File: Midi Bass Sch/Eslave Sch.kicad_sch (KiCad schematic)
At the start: 1 part

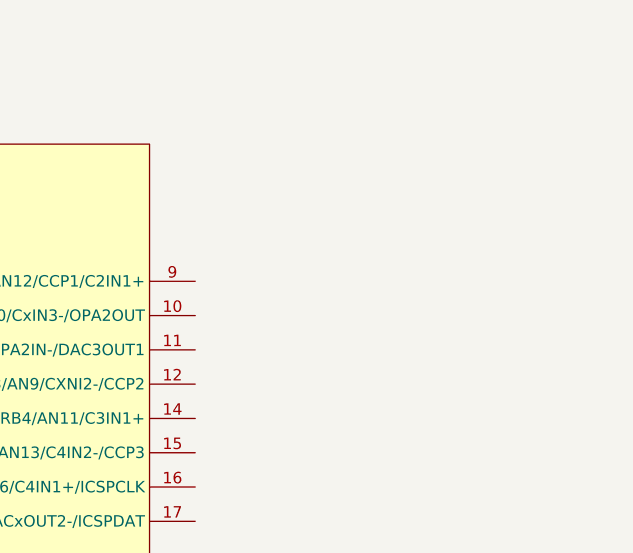
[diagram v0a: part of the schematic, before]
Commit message: reduced time of pulse
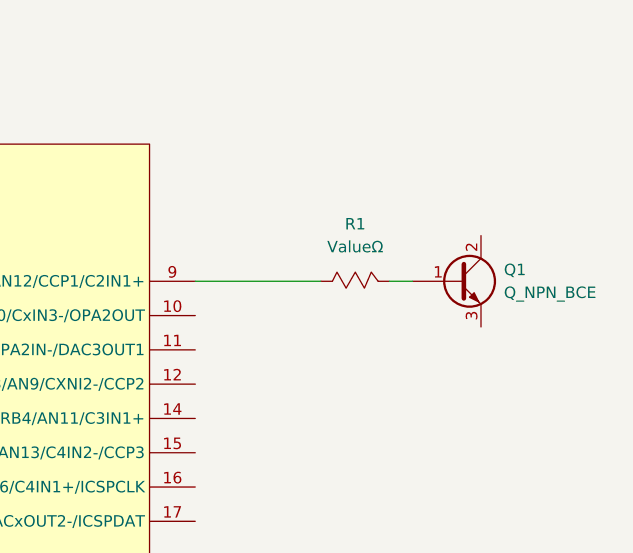
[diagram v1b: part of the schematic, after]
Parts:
- added Q1: Q_NPN_BCE, symbol Device:Q_NPN_BCE
- added R1: ValueΩ, symbol Custom Symbols:Resistor_Mod
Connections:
- net at U?.9 (RB0/AN12/CCP1/C2IN1+): now also R1.1
- new net: Q1.1 (B), R1.2
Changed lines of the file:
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@@
+	(wire
+		(pts
+			(xy 210.82 46.99) (xy 213.36 46.99)
+		)
+		(stroke
+			(width 0)
+			(type default)
+		)
+	)
 	(wire
 		(pts
@@
 		(pts
 			(xy 152.4 156.21) (xy 152.4 154.94)
+		)
+		(stroke
+			(width 0)
+			(type default)
+		)
+	)
+	(wire
+		(pts
+			(xy 189.23 46.99) (xy 203.2 46.99)
 		)
 		(stroke
@@
 				(justify right)
 				(hide yes)
+			)
+		)
+	)
+	(symbol
+		(lib_id "Custom Symbols:Resistor_Mod")
+		(at 207.01 46.99 0)
+		(unit 1)
+		(exclude_from_sim no)
+		(in_bom yes)
+		(on_board yes)
+		(dnp no)
+		(fields_autoplaced yes)
+		(property "Reference" "R1"
+			(at 207.01 40.64 0)
+			(effects
+				(font
+					(size 1.27 1.27)
+				)
+			)
+		)
+		(property "Value" "ValueΩ"
+			(at 207.01 43.18 0)
+			(effects
+				(font
+					(size 1.27 1.27)
+				)
+			)
+		)
+		(property "Footprint" ""
+			(at 205.74 44.45 0)
+			(effects
+				(font
+					(size 1.27 1.27)
+				)
+				(hide yes)
+			)
+		)
+		(property "Datasheet" ""
+			(at 205.74 44.45 0)
+			(effects
+				(font
+					(size 1.27 1.27)
+				)
+				(hide yes)
+			)
+		)
+		(property "Description" ""
+			(at 207.01 46.99 0)
+			(effects
+				(font
+					(size 1.27 1.27)
+				)
+				(hide yes)
+			)
+		)
+		(pin "2"
+		)
+		(pin "1"
+		)
+		(instances
+			(project ""
+				(path "/06818073-fb22-48ee-acc5-6dedd827034e/55f5fc9c-362b-429f-ad6f-f98ffe4c4860"
+					(reference "R1")
+					(unit 1)
+				)
 			)
 		)
@@
 					(unit 1)
 				)
+			)
+		)
+	)
+	(symbol
+		(lib_id "Device:Q_NPN_BCE")
+		(at 218.44 46.99 0)
+		(unit 1)
+		(exclude_from_sim no)
+		(in_bom yes)
+		(on_board yes)
+		(dnp no)
+		(fields_autoplaced yes)
+		(property "Reference" "Q1"
+			(at 223.52 45.7199 0)
+			(effects
+				(font
+					(size 1.27 1.27)
+				)
+				(justify left)
+			)
+		)
+		(property "Value" "Q_NPN_BCE"
+			(at 223.52 48.2599 0)
+			(effects
+				(font
+					(size 1.27 1.27)
+				)
+				(justify left)
+			)
+		)
+		(property "Footprint" ""
+			(at 223.52 44.45 0)
+			(effects
+				(font
+					(size 1.27 1.27)
+				)
+				(hide yes)
+			)
+		)
+		(property "Datasheet" "~"
+			(at 218.44 46.99 0)
+			(effects
+				(font
+					(size 1.27 1.27)
+				)
+				(hide yes)
+			)
+		)
+		(property "Description" "NPN transistor, base/collector/emitter"
+			(at 218.44 46.99 0)
+			(effects
+				(font
+					(size 1.27 1.27)
+				)
+				(hide yes)
+			)
+		)
+		(pin "1"
+		)
+		(pin "2"
+		)
+		(pin "3"
+		)
+		(instances
+			(project ""
+				(path "/06818073-fb22-48ee-acc5-6dedd827034e/55f5fc9c-362b-429f-ad6f-f98ffe4c4860"
+					(reference "Q1")
+					(unit 1)
+				)

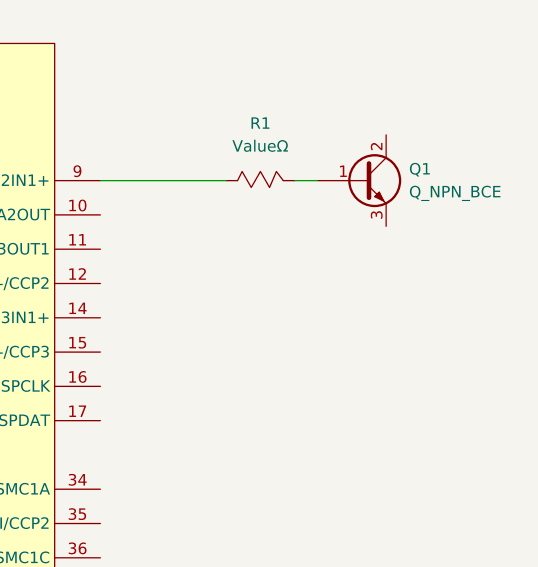
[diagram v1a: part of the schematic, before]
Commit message: updated schematic to include solenoid output
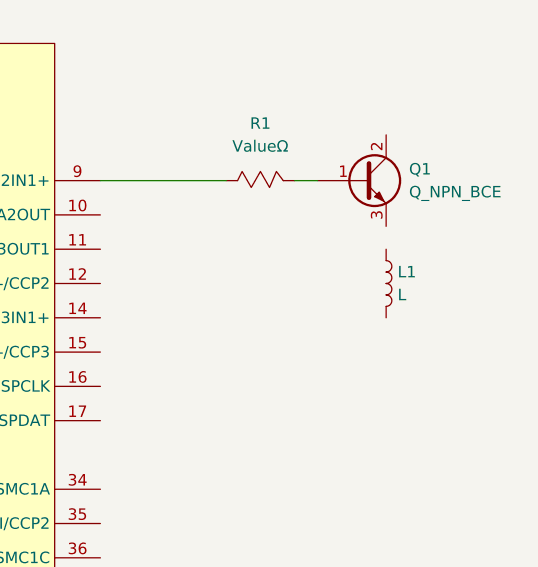
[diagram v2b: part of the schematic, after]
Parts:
- added L1: L, symbol Device:L
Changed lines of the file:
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@@
+	)
+	(symbol
+		(lib_id "Device:L")
+		(at 220.98 58.42 0)
+		(unit 1)
+		(exclude_from_sim no)
+		(in_bom yes)
+		(on_board yes)
+		(dnp no)
+		(fields_autoplaced yes)
+		(property "Reference" "L1"
+			(at 222.25 57.1499 0)
+			(effects
+				(font
+					(size 1.27 1.27)
+				)
+				(justify left)
+			)
+		)
+		(property "Value" "L"
+			(at 222.25 59.6899 0)
+			(effects
+				(font
+					(size 1.27 1.27)
+				)
+				(justify left)
+			)
+		)
+		(property "Footprint" ""
+			(at 220.98 58.42 0)
+			(effects
+				(font
+					(size 1.27 1.27)
+				)
+				(hide yes)
+			)
+		)
+		(property "Datasheet" "~"
+			(at 220.98 58.42 0)
+			(effects
+				(font
+					(size 1.27 1.27)
+				)
+				(hide yes)
+			)
+		)
+		(property "Description" "Inductor"
+			(at 220.98 58.42 0)
+			(effects
+				(font
+					(size 1.27 1.27)
+				)
+				(hide yes)
+			)
+		)
+		(pin "1"
+		)
+		(pin "2"
+		)
+		(instances
+			(project ""
+				(path "/06818073-fb22-48ee-acc5-6dedd827034e/55f5fc9c-362b-429f-ad6f-f98ffe4c4860"
+					(reference "L1")
+					(unit 1)
+				)
+			)
+		)
 	)
 	(symbol

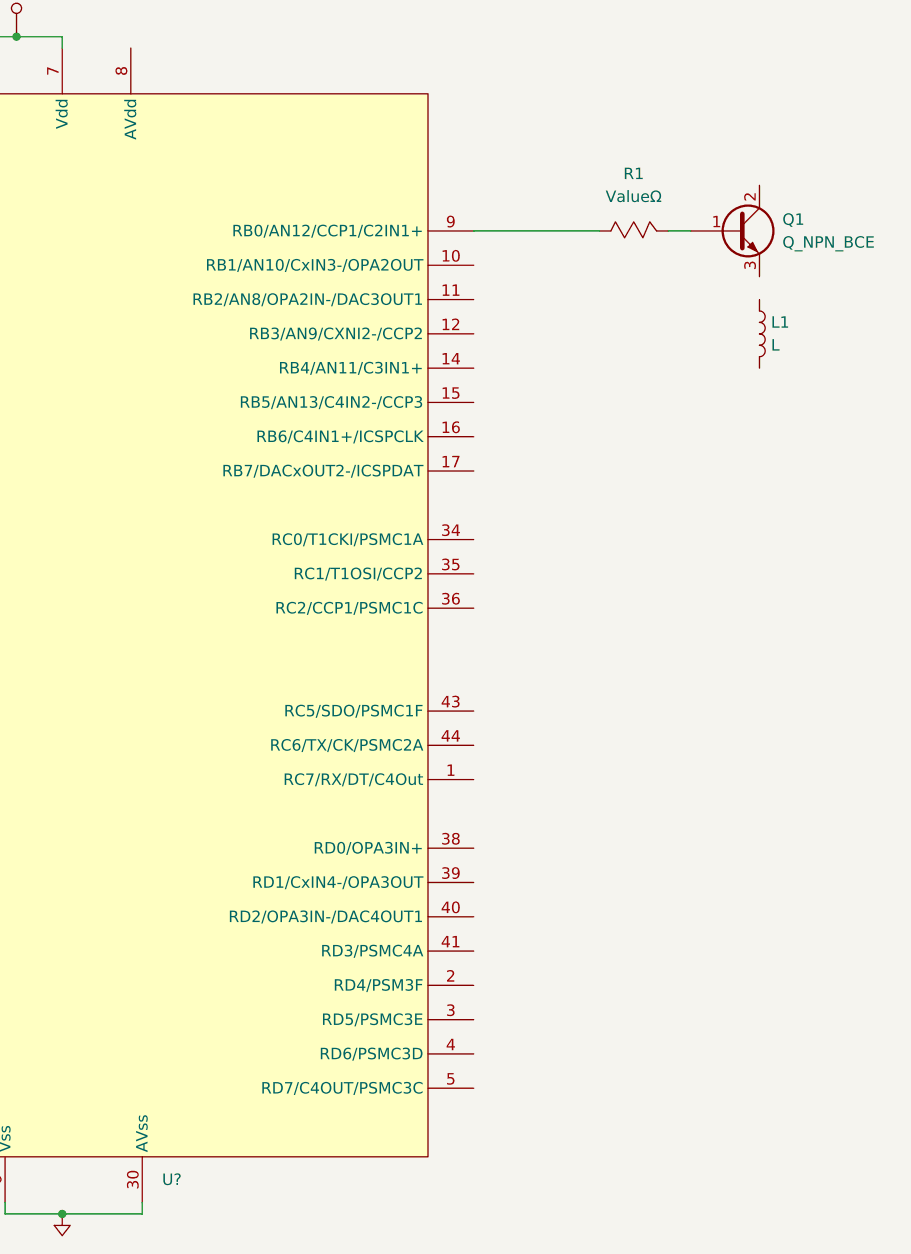
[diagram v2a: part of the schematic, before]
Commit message: updated schematic to include solenoids for pluck slave
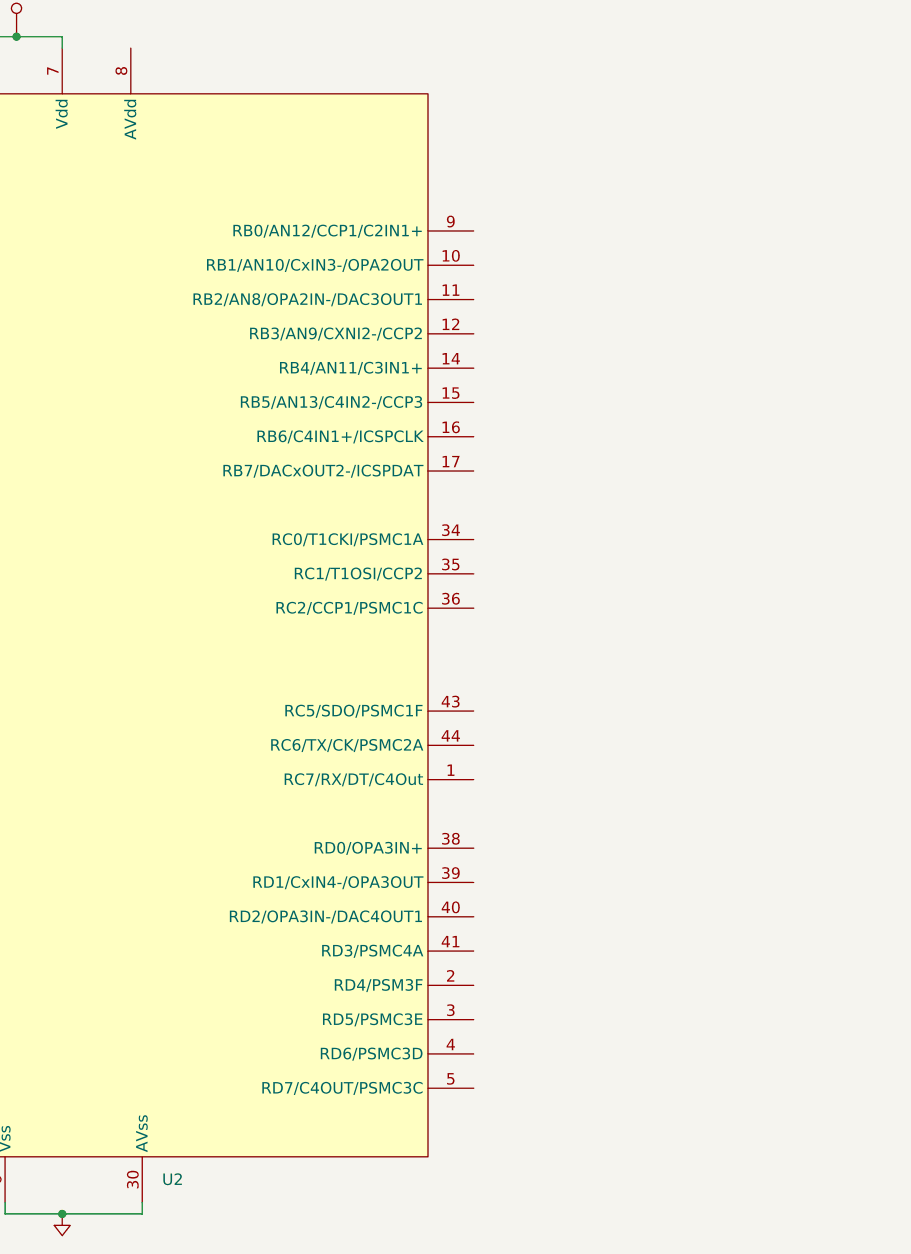
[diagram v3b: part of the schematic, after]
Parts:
- removed L1: L, symbol Device:L
- removed Q1: Q_NPN_BCE, symbol Device:Q_NPN_BCE
- removed R1: ValueΩ, symbol Custom Symbols:Resistor_Mod
- gave numbers to parts that had none: 1
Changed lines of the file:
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@@
-	(wire
-		(pts
-			(xy 210.82 46.99) (xy 213.36 46.99)
-		)
-		(stroke
-			(width 0)
-			(type default)
-		)
-	)
 	(wire
 		(pts
@@
 		(pts
 			(xy 152.4 156.21) (xy 152.4 154.94)
-		)
-		(stroke
-			(width 0)
-			(type default)
-		)
-	)
-	(wire
-		(pts
-			(xy 189.23 46.99) (xy 203.2 46.99)
 		)
 		(stroke
@@
 				(justify right)
 				(hide yes)
-			)
-		)
-	)
-	(symbol
-		(lib_id "Custom Symbols:Resistor_Mod")
-		(at 207.01 46.99 0)
-		(unit 1)
-		(exclude_from_sim no)
-		(in_bom yes)
-		(on_board yes)
-		(dnp no)
-		(fields_autoplaced yes)
-		(property "Reference" "R1"
-			(at 207.01 40.64 0)
-			(effects
-				(font
-					(size 1.27 1.27)
-				)
-			)
-		)
-		(property "Value" "ValueΩ"
-			(at 207.01 43.18 0)
-			(effects
-				(font
-					(size 1.27 1.27)
-				)
-			)
-		)
-		(property "Footprint" ""
-			(at 205.74 44.45 0)
-			(effects
-				(font
-					(size 1.27 1.27)
-				)
-				(hide yes)
-			)
-		)
-		(property "Datasheet" ""
-			(at 205.74 44.45 0)
-			(effects
-				(font
-					(size 1.27 1.27)
-				)
-				(hide yes)
-			)
-		)
-		(property "Description" ""
-			(at 207.01 46.99 0)
-			(effects
-				(font
-					(size 1.27 1.27)
-				)
-				(hide yes)
-			)
-		)
-		(pin "2"
-		)
-		(pin "1"
-		)
-		(instances
-			(project ""
-				(path "/06818073-fb22-48ee-acc5-6dedd827034e/55f5fc9c-362b-429f-ad6f-f98ffe4c4860"
-					(reference "R1")
-					(unit 1)
-				)
 			)
 		)
@@
 	)
 	(symbol
-		(lib_id "Device:L")
-		(at 220.98 58.42 0)
-		(unit 1)
-		(exclude_from_sim no)
-		(in_bom yes)
-		(on_board yes)
-		(dnp no)
-		(fields_autoplaced yes)
-		(property "Reference" "L1"
-			(at 222.25 57.1499 0)
-			(effects
-				(font
-					(size 1.27 1.27)
-				)
-				(justify left)
-			)
-		)
-		(property "Value" "L"
-			(at 222.25 59.6899 0)
-			(effects
-				(font
-					(size 1.27 1.27)
-				)
-				(justify left)
-			)
-		)
-		(property "Footprint" ""
-			(at 220.98 58.42 0)
-			(effects
-				(font
-					(size 1.27 1.27)
-				)
-				(hide yes)
-			)
-		)
-		(property "Datasheet" "~"
-			(at 220.98 58.42 0)
-			(effects
-				(font
-					(size 1.27 1.27)
-				)
-				(hide yes)
-			)
-		)
-		(property "Description" "Inductor"
-			(at 220.98 58.42 0)
-			(effects
-				(font
-					(size 1.27 1.27)
-				)
-				(hide yes)
-			)
-		)
-		(pin "1"
-		)
-		(pin "2"
-		)
-		(instances
-			(project ""
-				(path "/06818073-fb22-48ee-acc5-6dedd827034e/55f5fc9c-362b-429f-ad6f-f98ffe4c4860"
-					(reference "L1")
-					(unit 1)
-				)
-			)
-		)
-	)
-	(symbol
-		(lib_id "Device:Q_NPN_BCE")
-		(at 218.44 46.99 0)
-		(unit 1)
-		(exclude_from_sim no)
-		(in_bom yes)
-		(on_board yes)
-		(dnp no)
-		(fields_autoplaced yes)
-		(property "Reference" "Q1"
-			(at 223.52 45.7199 0)
-			(effects
-				(font
-					(size 1.27 1.27)
-				)
-				(justify left)
-			)
-		)
-		(property "Value" "Q_NPN_BCE"
-			(at 223.52 48.2599 0)
-			(effects
-				(font
-					(size 1.27 1.27)
-				)
-				(justify left)
-			)
-		)
-		(property "Footprint" ""
-			(at 223.52 44.45 0)
-			(effects
-				(font
-					(size 1.27 1.27)
-				)
-				(hide yes)
-			)
-		)
-		(property "Datasheet" "~"
-			(at 218.44 46.99 0)
-			(effects
-				(font
-					(size 1.27 1.27)
-				)
-				(hide yes)
-			)
-		)
-		(property "Description" "NPN transistor, base/collector/emitter"
-			(at 218.44 46.99 0)
-			(effects
-				(font
-					(size 1.27 1.27)
-				)
-				(hide yes)
-			)
-		)
-		(pin "1"
-		)
-		(pin "2"
-		)
-		(pin "3"
-		)
-		(instances
-			(project ""
-				(path "/06818073-fb22-48ee-acc5-6dedd827034e/55f5fc9c-362b-429f-ad6f-f98ffe4c4860"
-					(reference "Q1")
-					(unit 1)
-				)
-			)
-		)
-	)
-	(symbol
 		(lib_id "Owen's Symbols:PIC16F1789_44")
 		(at 143.51 31.75 0)
@@
 		(dnp no)
 		(fields_autoplaced yes)
-		(property "Reference" "U?"
+		(property "Reference" "U2"
 			(at 154.5941 152.4 0)
 			(effects
@@
 			(project "Midi Bass Sch"
 				(path "/06818073-fb22-48ee-acc5-6dedd827034e/55f5fc9c-362b-429f-ad6f-f98ffe4c4860"
-					(reference "U?")
+					(reference "U2")
 					(unit 1)
 				)

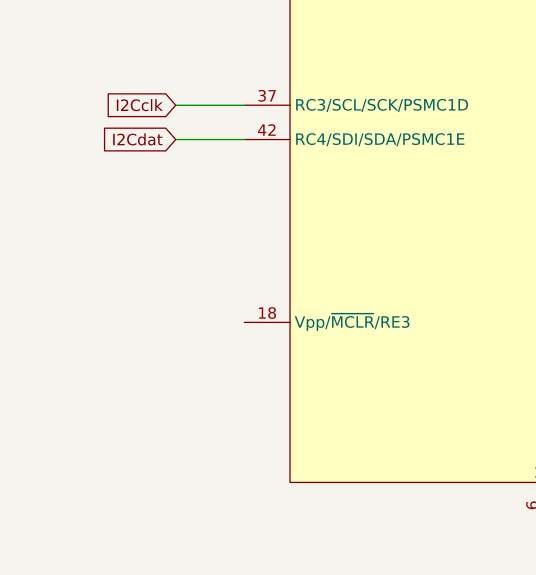
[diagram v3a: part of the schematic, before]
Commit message: added startup clear to schematic
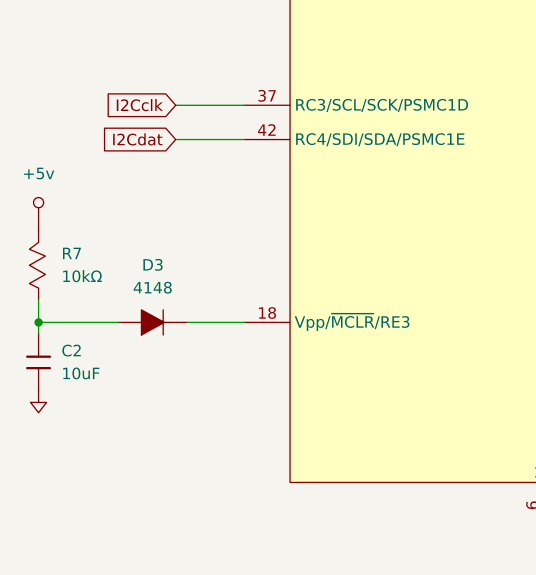
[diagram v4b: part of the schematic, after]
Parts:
- added C2: 10uF, symbol Owen's Symbols:Capacitor
- added D3: 4148, symbol Owen's Symbols:Diode
- added R7: 10kΩ, symbol Owen's Symbols:Resistor_Mod
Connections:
- net +5v: now also R7.2
- net GND: now also C2.2
- net at U2.18 (Vpp/~{MCLR}/RE3): now also D3.2
- new net: C2.1, D3.1, R7.1

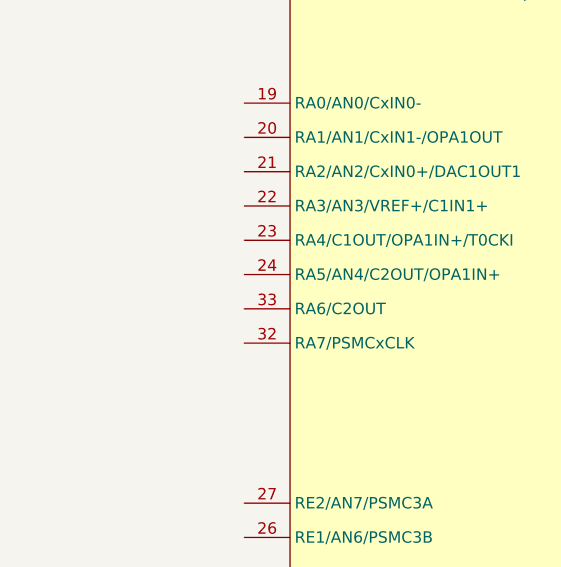
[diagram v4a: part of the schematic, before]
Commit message: updated schematic to include test points for pics
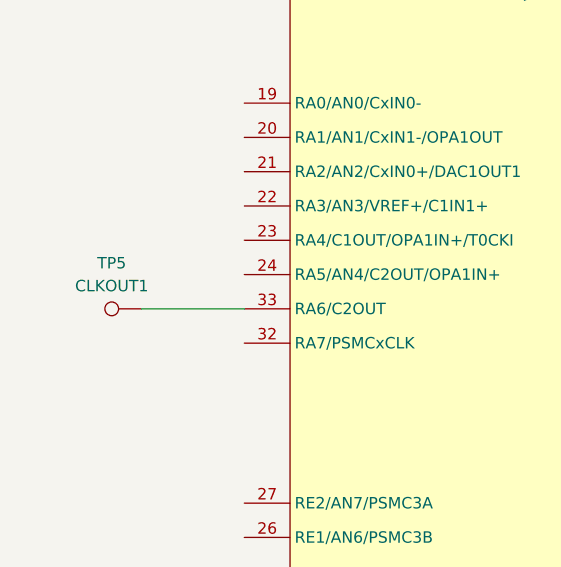
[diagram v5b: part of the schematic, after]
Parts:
- added TP5: CLKOUT1, symbol Connector:TestPoint
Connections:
- net at U2.33 (RA6/C2OUT): now also TP5.1
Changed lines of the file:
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@@
+		)
+	)
+	(wire
+		(pts
+			(xy 92.71 69.85) (xy 104.14 69.85)
+		)
+		(stroke
+			(width 0)
+			(type default)
 		)
 	)
@@
 			)
 		)
+	)
+	(symbol
+		(lib_id "Connector:TestPoint")
+		(at 92.71 69.85 90)
+		(unit 1)
+		(exclude_from_sim no)
+		(in_bom yes)
+		(on_board yes)
+		(dnp no)
+		(fields_autoplaced yes)
+		(property "Reference" "TP5"
+			(at 89.408 64.77 90)
+			(effects
+				(font
+					(size 1.27 1.27)
+				)
+			)
+		)
+		(property "Value" "CLKOUT1"
+			(at 89.408 67.31 90)
+			(effects
+				(font
+					(size 1.27 1.27)
+				)
+			)
+		)
+		(property "Footprint" ""
+			(at 92.71 64.77 0)
+			(effects
+				(font
+					(size 1.27 1.27)
+				)
+				(hide yes)
+			)
+		)
+		(property "Datasheet" "~"
+			(at 92.71 64.77 0)
+			(effects
+				(font
+					(size 1.27 1.27)
+				)
+				(hide yes)
+			)
+		)
+		(property "Description" "test point"
+			(at 92.71 69.85 0)
+			(effects
+				(font
+					(size 1.27 1.27)
+				)
+				(hide yes)
+			)
+		)
+		(pin "1"
+		)
+		(instances
+			(project "Midi Bass Sch"
+				(path "/06818073-fb22-48ee-acc5-6dedd827034e/55f5fc9c-362b-429f-ad6f-f98ffe4c4860"
+					(reference "TP5")
+					(unit 1)
+				)
+			)
+		)
